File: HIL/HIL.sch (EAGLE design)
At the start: 247 parts, among them J1 JTAG_ARM_10PIN, J4 JTAG_ARM_10PIN, U1 CD74HC4067SM96, U10 INA219AIDCNR, U11 INA219AIDCNR, U12 INA219AIDCNR, U13 TM4C1294NCPDT, U14 ADUM1201ARZ, U15 SN65HVD230D, U16 TL1963AKTTR., U17 FT230XS, U2 TL1963AKTTR., U3 CD74HC4067SM96, U4 CD74HC4067SM96, U5 MCP4725A0T-E/CH, U6 TL1963AKTTR., U7 MCP2003-E/SN, U9 INA219AIDCNR, X1 A1944-50, X2 A1944-50, X4 A1944-50, Y3 NX3225GA

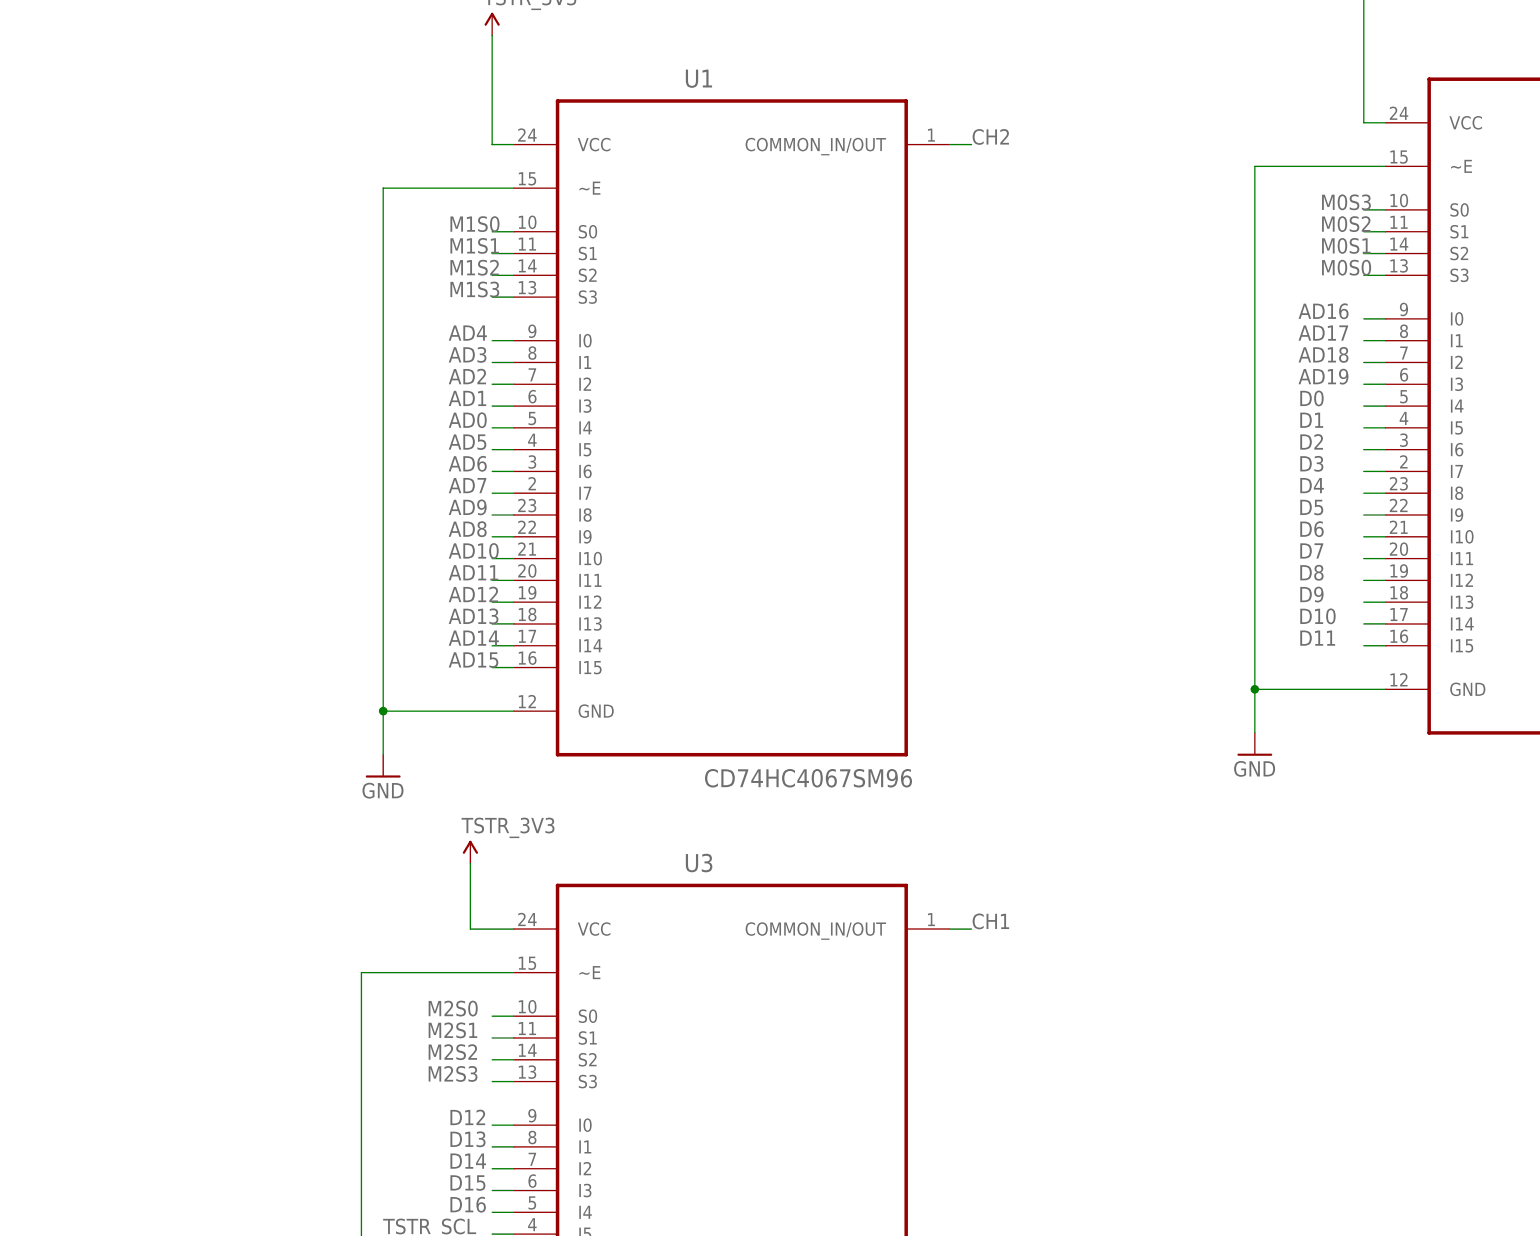
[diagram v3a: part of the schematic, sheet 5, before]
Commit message: Generate pdfs, and gerbers Libraries “>NAME” parameter change
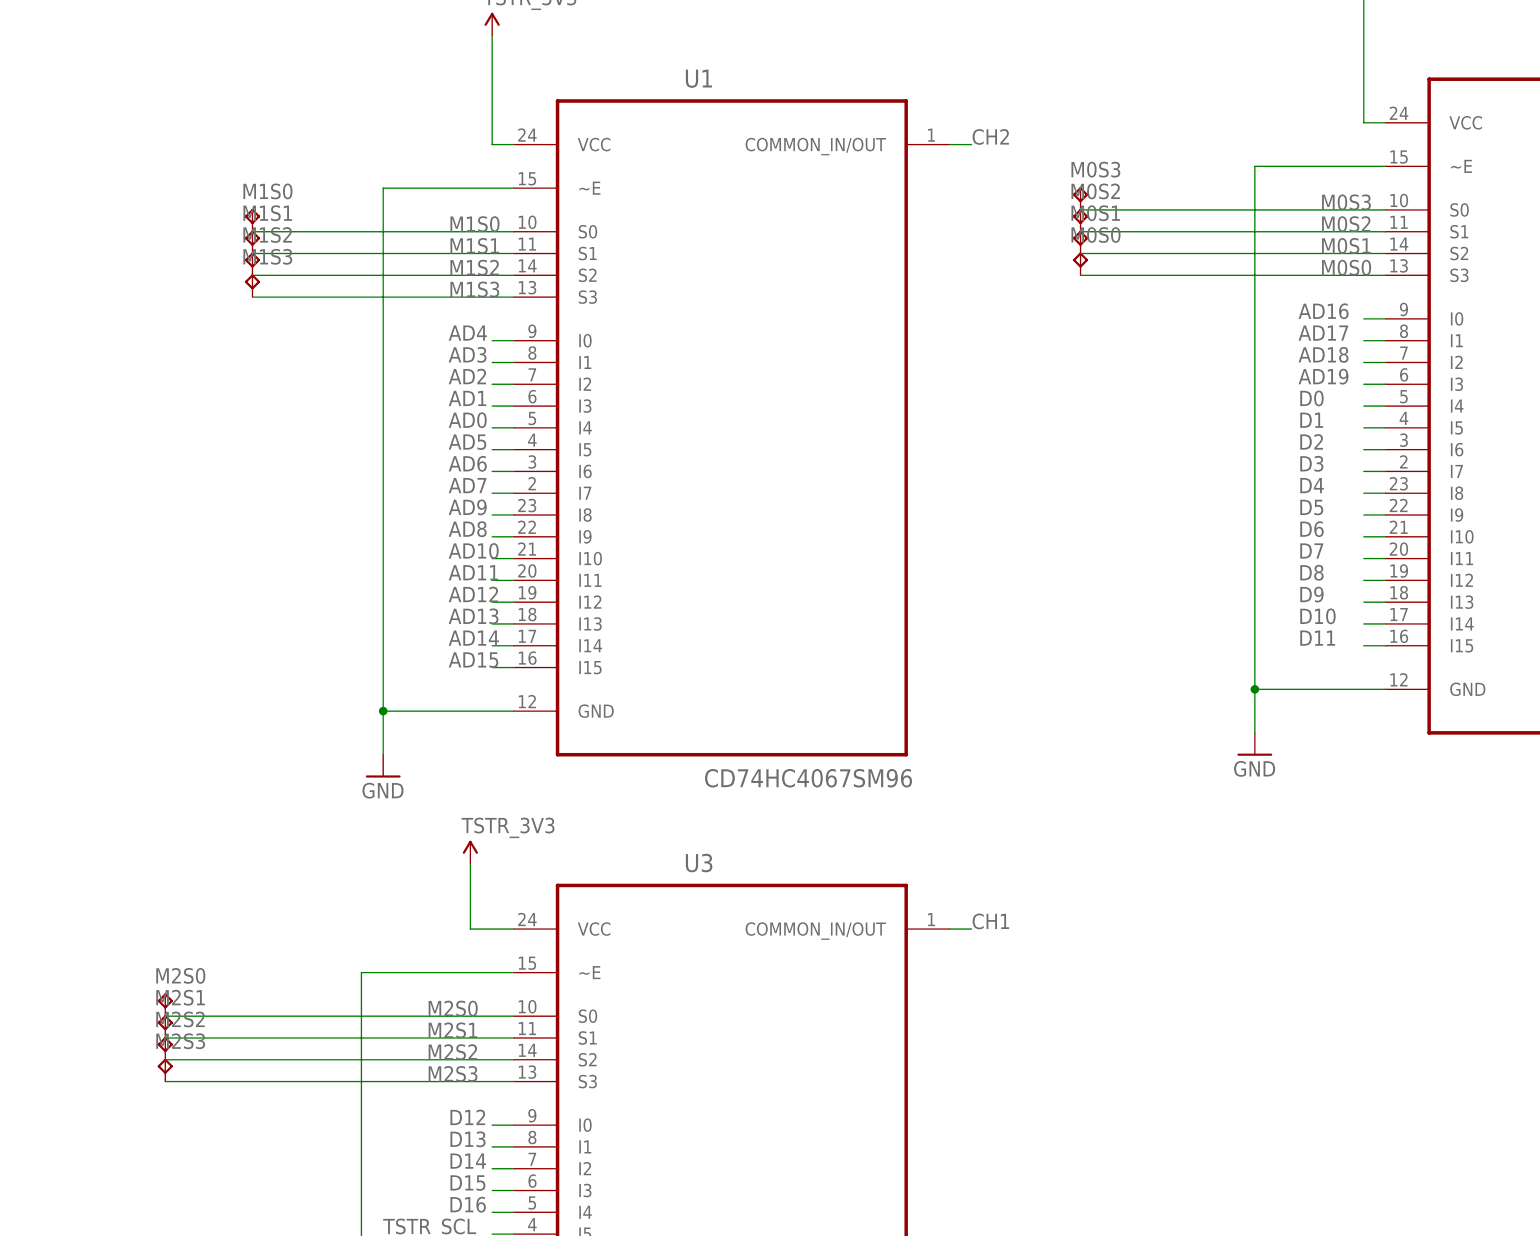
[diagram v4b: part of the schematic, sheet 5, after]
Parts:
- added DEBUGONLY: (no value), JDT-1800_smahed:PINHD-1X15
- added JP18: (no value), JDT-1800_smahed:PINHD-1X3CB
- added M0S0, M0S1, M0S2, M0S3: TPB1,27, testpad:TPB1,27
- added M1S0, M1S1, M1S2, M1S3, M2S0, M2S1, M2S2, M2S3: M0S3, testpad:TPB1,27
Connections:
- net GND: now also DEBUGONLY.14, DEBUGONLY.15
- net LDO1_ENABLE: now also JP18.1
- net LDO2_ENABLE: now also JP18.2
- net LDO3_ENABLE: now also JP18.3
- net M0S0: now also M0S0.TP
- net M0S1: now also M0S1.TP
- net M0S2: now also M0S2.TP
- net M0S3: now also M0S3.TP
- net M1S0: now also M1S0.TP
- net M1S1: now also M1S1.TP
- net M1S2: now also M1S2.TP
- net M1S3: now also M1S3.TP
- net M2S0: now also M2S0.TP
- net M2S1: now also M2S1.TP
- net M2S2: now also M2S2.TP
- net M2S3: now also M2S3.TP

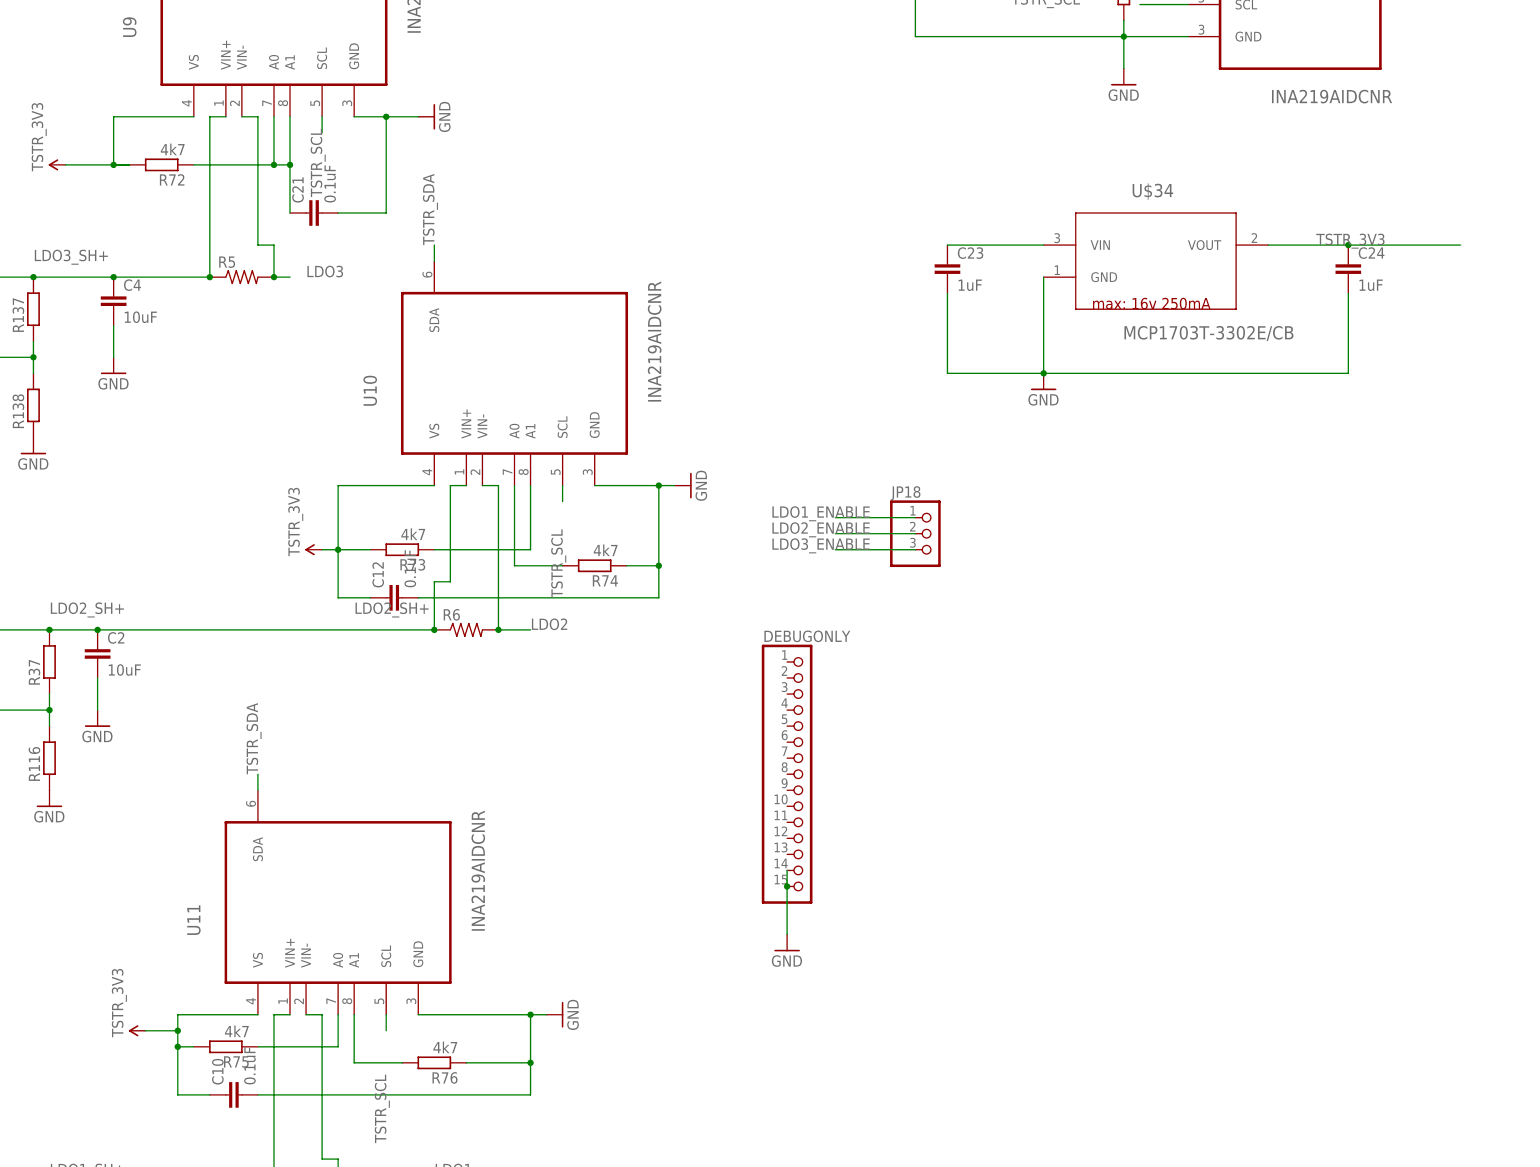
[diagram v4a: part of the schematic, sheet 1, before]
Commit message: Fix:   - Vcc pin present in the schematic Add: - digital tersistor to the schematic          - measurements of the holes/drills
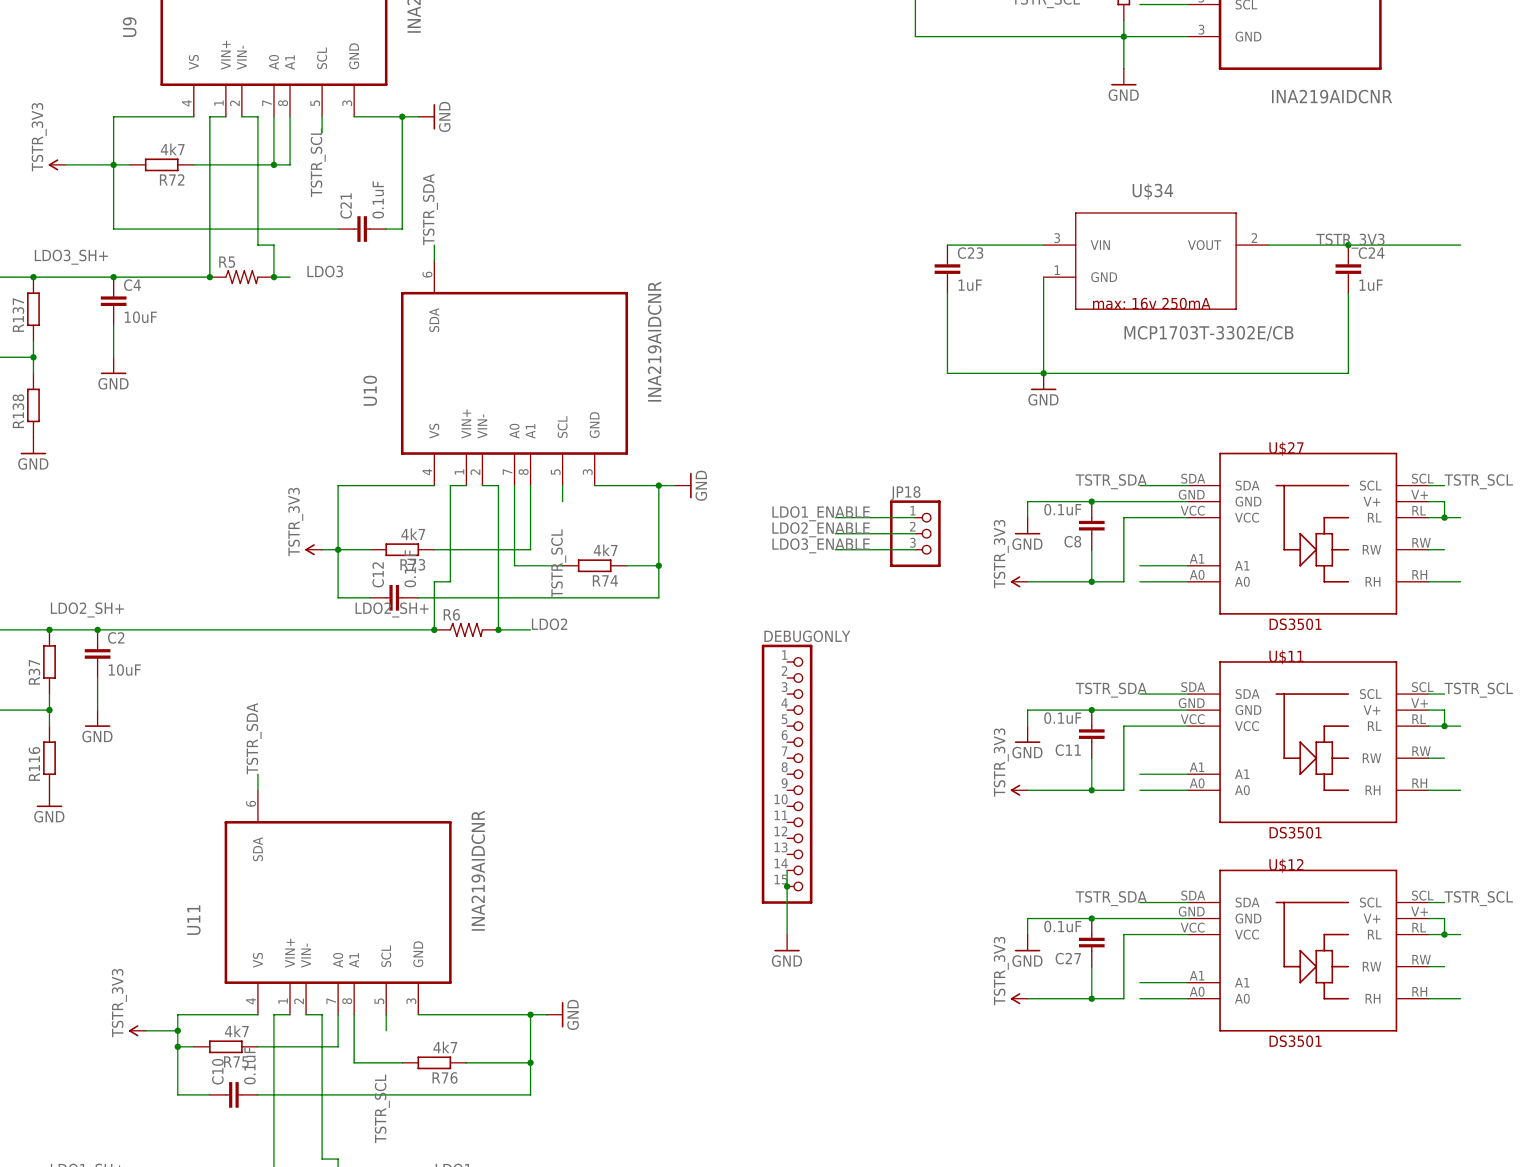
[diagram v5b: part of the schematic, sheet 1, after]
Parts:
- added C11, C27, C8: 0.1uF, rcl:C-EUC0402
- added U$11, U$12, U$27: DS3501, Digital resistor:DS3501
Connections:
- removed net VCC: R72.2, U9.VS
- new net AS: R72.1, U9.A0, U9.A1
- new net N$53: U$11.A1
- new net N$54: U$11.A0
- new net N$55: U$11.RH
- new net N$56: U$11.RW
- new net N$57: U$11.RL, U$11.V+
- new net N$63: U$12.A1
- new net N$66: U$12.A0
- new net N$67: U$12.RH
- new net N$68: U$12.RW
- new net N$69: U$12.RL, U$12.V+
- new net N$70: U$27.A1
- new net N$71: U$27.A0
- new net N$72: U$27.RH
- new net N$73: U$27.RW
- new net N$74: U$27.RL, U$27.V+
- net GND: now also C11.2, C27.2, C8.2, U$11.GND, U$12.GND, U$27.GND
- net TSTR_3V3: now also C11.1, C27.1, C8.1, R72.2, U$11.VCC, U$12.VCC, U$27.VCC, U9.VS; no longer R72.1, U9.A0, U9.A1
- net TSTR_SCL: now also U$11.SCL, U$12.SCL, U$27.SCL
- net TSTR_SDA: now also U$11.SDA, U$12.SDA, U$27.SDA
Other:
- moved on the sheet: C21
